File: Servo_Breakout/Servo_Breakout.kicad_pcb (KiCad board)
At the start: 4 copper layers, 96.5 x 31 mm, 52 parts, among them J101 395221002, J102 Conn_01x03, J103 Conn_01x04, Q101 2N7002, U101 TVS0500DRV, U301 STPS15H100CBY-TR, U302 BD9G500EFJ-LAE2, U401 TXS0102DCT, U501 ICM7555xP, U502 TPL0401A-10-Q1

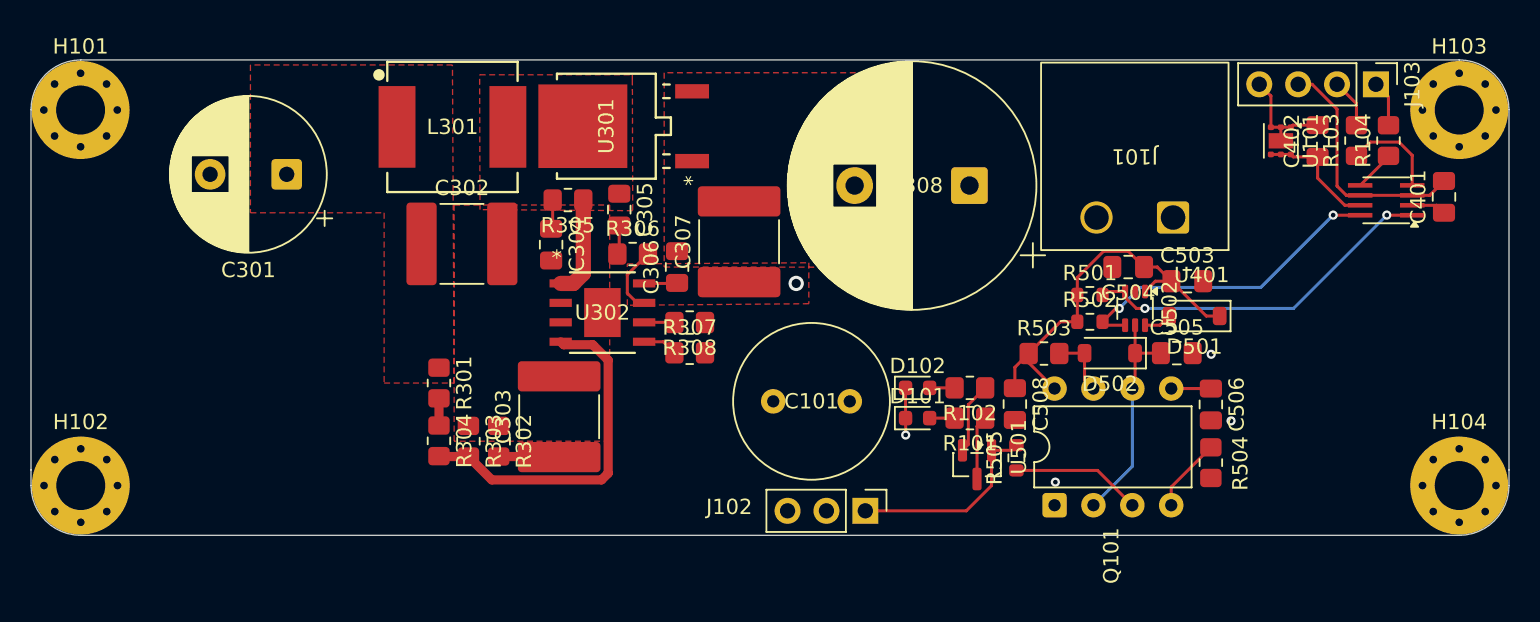
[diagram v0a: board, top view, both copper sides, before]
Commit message: Finalized layout and silkscreen
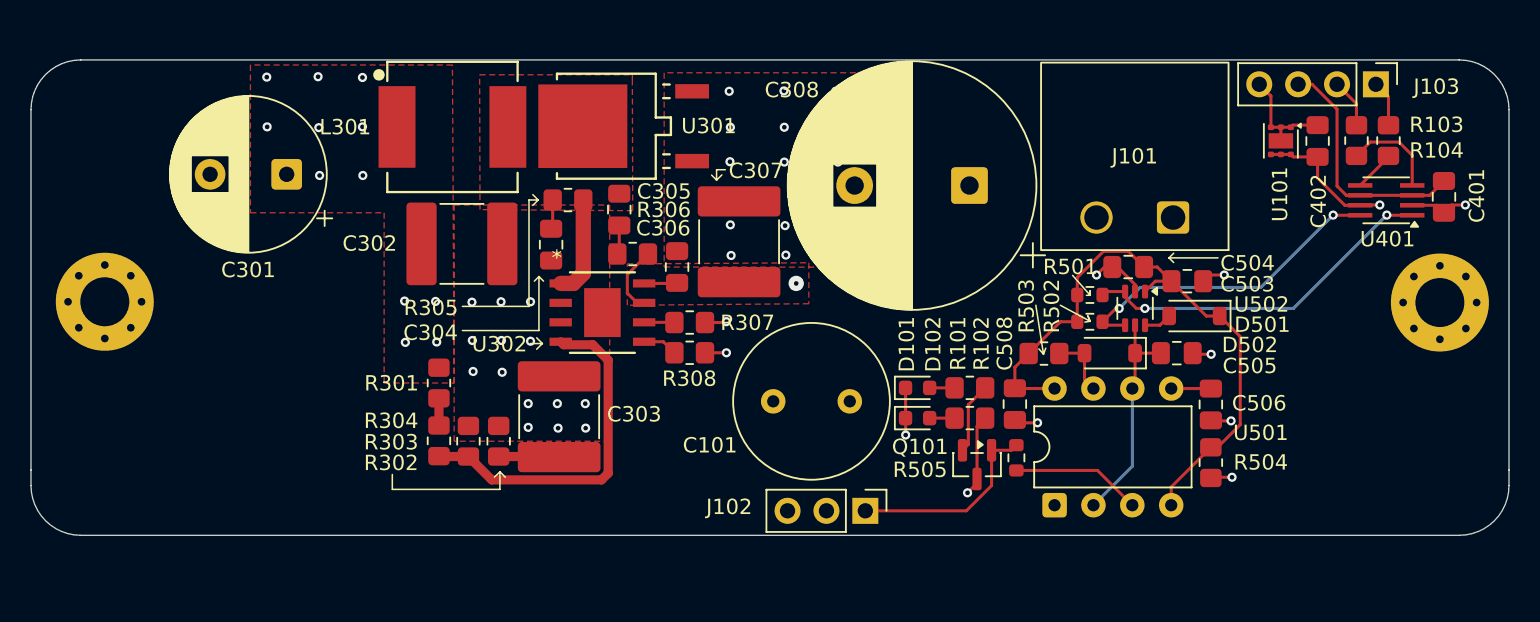
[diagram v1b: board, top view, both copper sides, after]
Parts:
- removed the H101 at (58.9, 54.2)
- removed H103: M3, MountingHole:MountingHole_3.2mm_M3_Pad_Via
- moved H101 12.1 mm to (60.5, 66.8)
- moved H102 12.0 mm to (147.7, 66.8)
- renumbered H102 to H101, H104 to H102
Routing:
- net GND: track 16.4 -> 30.1 mm, vias 4 -> 38
- net /Timer/VCC: track 31.2 -> 41.0 mm
- net /VBUCK: track 12.2 -> 16.1 mm, vias 0 -> 15

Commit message: quick improvement to +36 pour clearance
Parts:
- moved R307 0.70 mm to (98.7, 70.8)
- moved R308 0.70 mm to (98.7, 68.8)
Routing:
- net Net-(U302-FB): track 22.9 -> 28.5 mm
- net Net-(U302-BOOT): track 4.48 -> 8.79 mm, vias 0 -> 2
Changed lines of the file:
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@@
 	(footprint "Resistor_SMD:R_0805_2012Metric_Pad1.20x1.40mm_HandSolder"
 		(layer "F.Cu")
-		(at 98.695 68.129 180)
+		(at 98.675 68.825 180)
 		(descr "Resistor SMD 0805 (2012 Metric), square (rectangular) end terminal, IPC-7351 nominal with elongated pad for handsoldering. (Body size source: IPC-SM-782 page 72, https://www.pcb-3d.com/wordpress/wp-content/uploads/ipc-sm-782a_amendment_1_and_2.pdf), generated with kicad-footprint-generator")
 		(tags "resistor handsolder")
@@
 	(footprint "Resistor_SMD:R_0805_2012Metric_Pad1.20x1.40mm_HandSolder"
 		(layer "F.Cu")
-		(at 98.695 70.104)
+		(at 98.675 70.8)
 		(descr "Resistor SMD 0805 (2012 Metric), square (rectangular) end terminal, IPC-7351 nominal with elongated pad for handsoldering. (Body size source: IPC-SM-782 page 72, https://www.pcb-3d.com/wordpress/wp-content/uploads/ipc-sm-782a_amendment_1_and_2.pdf), generated with kicad-footprint-generator")
 		(tags "resistor handsolder")
@@
 	)
 	(segment
-		(start 147.955 60.96)
-		(end 147.4675 60.4725)
+		(start 99.675 68.825)
+		(end 101.074 68.825)
 		(width 0.2)
 		(layer "F.Cu")
@@
 	)
 	(segment
-		(start 99.695 70.104)
-		(end 101.092 70.104)
+		(start 147.955 60.96)
+		(end 147.4675 60.4725)
 		(width 0.2)
 		(layer "F.Cu")
@@
 	)
 	(segment
-		(start 99.695 68.129)
-		(end 101.035 68.129)
+		(start 101.074 68.825)
+		(end 101.092 68.843)
 		(width 0.2)
 		(layer "F.Cu")
@@
 	)
 	(segment
-		(start 101.035 68.129)
-		(end 101.092 68.072)
-		(width 0.2)
-		(layer "F.Cu")
-		(net 1)
-	)
-	(segment
 		(start 132.7653 74.55)
 		(end 132.7313 74.516)
@@
 	)
 	(segment
+		(start 99.675 70.8)
+		(end 101.017 70.8)
+		(width 0.2)
+		(layer "F.Cu")
+		(net 1)
+	)
+	(segment
 		(start 127.7813 66.1035)
 		(end 127.7813 65.653501)
@@
 		(net 1)
 	)
+	(segment
+		(start 101.017 70.8)
+		(end 101.092 70.875)
+		(width 0.2)
+		(layer "F.Cu")
+		(net 1)
+	)
 	(via
 		(at 101.4 63.75)
@@
 	)
 	(via
-		(at 101.092 70.104)
+		(at 101.092 70.875)
 		(size 0.6)
 		(drill 0.3)
@@
 	)
 	(via
-		(at 101.092 68.072)
+		(at 101.092 68.843)
 		(size 0.6)
 		(drill 0.3)
@@
 	)
 	(segment
-		(start 95.719752 68.114)
-		(end 97.68 68.114)
+		(start 96.964 68.114)
+		(end 97.675 68.825)
 		(width 0.2)
 		(layer "F.Cu")
@@
 	)
 	(segment
-		(start 97.68 68.114)
-		(end 97.695 68.129)
+		(start 95.719752 68.114)
+		(end 96.964 68.114)
 		(width 0.2)
 		(layer "F.Cu")
@@
 	)
 	(segment
-		(start 84.245 76.879)
-		(end 82.345 76.879)
+		(start 90.359 69.384)
+		(end 90.9 69.925)
 		(width 0.6)
 		(layer "F.Cu")
@@
 	)
 	(segment
-		(start 93.371 77.972002)
-		(end 92.938002 78.405)
+		(start 82.32 76.854)
+		(end 84.22 76.854)
 		(width 0.6)
 		(layer "F.Cu")
@@
 	)
 	(segment
-		(start 92.938002 78.405)
-		(end 85.771 78.405)
+		(start 84.245 77.82)
+		(end 84.245 76.879)
 		(width 0.6)
 		(layer "F.Cu")
@@
 	)
 	(segment
-		(start 93.371 70.585998)
-		(end 93.371 77.972002)
+		(start 86.75 80.325)
+		(end 84.245 77.82)
 		(width 0.6)
 		(layer "F.Cu")
@@
 	)
 	(segment
-		(start 92.365202 69.5802)
-		(end 93.371 70.585998)
+		(start 84.22 76.854)
+		(end 84.245 76.879)
 		(width 0.6)
 		(layer "F.Cu")
@@
 	)
 	(segment
-		(start 85.771 78.405)
-		(end 84.245 76.879)
+		(start 93.35 80.325)
+		(end 86.75 80.325)
 		(width 0.6)
 		(layer "F.Cu")
@@
 	(segment
 		(start 90.270248 69.384)
-		(end 90.466448 69.5802)
+		(end 90.359 69.384)
 		(width 0.6)
 		(layer "F.Cu")
@@
 	)
 	(segment
-		(start 90.466448 69.5802)
-		(end 92.365202 69.5802)
+		(start 90.9 69.925)
+		(end 93.575 69.925)
 		(width 0.6)
 		(layer "F.Cu")
@@
 	)
 	(segment
-		(start 82.345 76.879)
-		(end 82.32 76.854)
+		(start 95.35 71.7)
+		(end 95.35 78.325)
 		(width 0.6)
 		(layer "F.Cu")
@@
 	)
 	(segment
-		(start 95.97 63.654)
-		(end 94.62 65.004)
+		(start 95.35 78.325)
+		(end 93.35 80.325)
+		(width 0.6)
+		(layer "F.Cu")
+		(net 44)
+	)
+	(segment
+		(start 93.575 69.925)
+		(end 95.35 71.7)
+		(width 0.6)
+		(layer "F.Cu")
+		(net 44)
+	)
+	(segment
+		(start 95.719752 66.969752)
+		(end 95.9 67.15)
 		(width 0.2)
 		(layer "F.Cu")
@@
 	)
 	(segment
-		(start 94.62 65.004)
-		(end 94.62 66.208398)
+		(start 95.9 67.15)
+		(end 96.1 67.35)
 		(width 0.2)
 		(layer "F.Cu")
@@
 	)
 	(segment
-		(start 94.62 66.208398)
-		(end 95.255602 66.844)
+		(start 96.1 67.35)
+		(end 97.1 67.35)
+		(width 0.2)
+		(layer "F.Cu")
+		(net 45)
+	)
+	(segment
+		(start 95.719752 66.844)
+		(end 95.719752 66.969752)
+		(width 0.2)
+		(layer "F.Cu")
+		(net 45)
+	)
+	(segment
+		(start 95.97 63.654)
+		(end 95.97 62.405)
 		(width 0.2)
 		(layer "F.Cu")
@@
 		(net 45)
 	)
+	(via
+		(at 97.1 67.35)
+		(size 0.6)
+		(drill 0.3)
+		(layers "F.Cu" "B.Cu")
+		(net 45)
+	)
+	(via
+		(at 95.97 62.405)
+		(size 0.6)
+		(drill 0.3)
+		(layers "F.Cu" "B.Cu")
+		(net 45)
+	)
 	(segment
-		(start 95.719752 69.384)
-		(end 96.975 69.384)
+		(start 97.1 67.35)
+		(end 97.1 63.535)
+		(width 0.2)
+		(layer "B.Cu")
+		(net 45)
+	)
+	(segment
+		(start 97.1 63.535)
+		(end 95.97 62.405)
+		(width 0.2)
+		(layer "B.Cu")
+		(net 45)
+	)
+	(segment
+		(start 96.259 69.384)
+		(end 97.675 70.8)
 		(width 0.2)
 		(layer "F.Cu")
@@
 	)
 	(segment
-		(start 96.975 69.384)
-		(end 97.695 70.104)
+		(start 95.719752 69.384)
+		(end 96.259 69.384)
 		(width 0.2)
 		(layer "F.Cu")
@@
 		(priority 6)
 		(connect_pads yes
-			(clearance 0)
+			(clearance 0.5)
 		)
 		(min_thickness 0.25)
@@
 		(hatch edge 0.5)
 		(connect_pads yes
-			(clearance 0)
+			(clearance 0.5)
 		)
 		(min_thickness 0.25)
@@
 		(polygon
 			(pts
-				(xy 94.62 64.3) (xy 106.475 64.225) (xy 106.475 66.9) (xy 94.62 67)
+				(xy 94.62 64.3) (xy 106.475 64.225) (xy 106.475 66.45) (xy 94.62 66.55)
 			)
 		)
@@
 		(priority 3)
 		(connect_pads yes
-			(clearance 0)
+			(clearance 0.4)
 		)
-		(min_thickness 0.25)
+		(min_thickness 0.4)
 		(filled_areas_thickness no)
 		(fill yes
@@
 		(priority 2)
 		(connect_pads yes
-			(clearance 0)
+			(clearance 0.4)
 		)
-		(min_thickness 0.25)
+		(min_thickness 0.4)
 		(filled_areas_thickness no)
 		(fill yes
@@
 		(priority 4)
 		(connect_pads yes
-			(clearance 0)
+			(clearance 0.4)
 		)
-		(min_thickness 0.25)
+		(min_thickness 0.4)
 		(filled_areas_thickness no)
 		(fill yes
@@
 		(priority 5)
 		(connect_pads yes
-			(clearance 0)
+			(clearance 0.25)
 		)
 		(min_thickness 0.25)
@@
 		(priority 5)
 		(connect_pads yes
-			(clearance 0)
+			(clearance 0.25)
 		)
 		(min_thickness 0.25)
@@
 		(priority 1)
 		(connect_pads yes
-			(clearance 0)
+			(clearance 0.25)
 		)
 		(min_thickness 0.25)
@@
 		(polygon
 			(pts
-				(xy 113.275 50.975) (xy 113.3 63.375) (xy 133.875 63.375) (xy 133.875 50.975)
+				(xy 113.25 63.4) (xy 113.25 55) (xy 133.875 55) (xy 133.825 63.4)
 			)
 		)

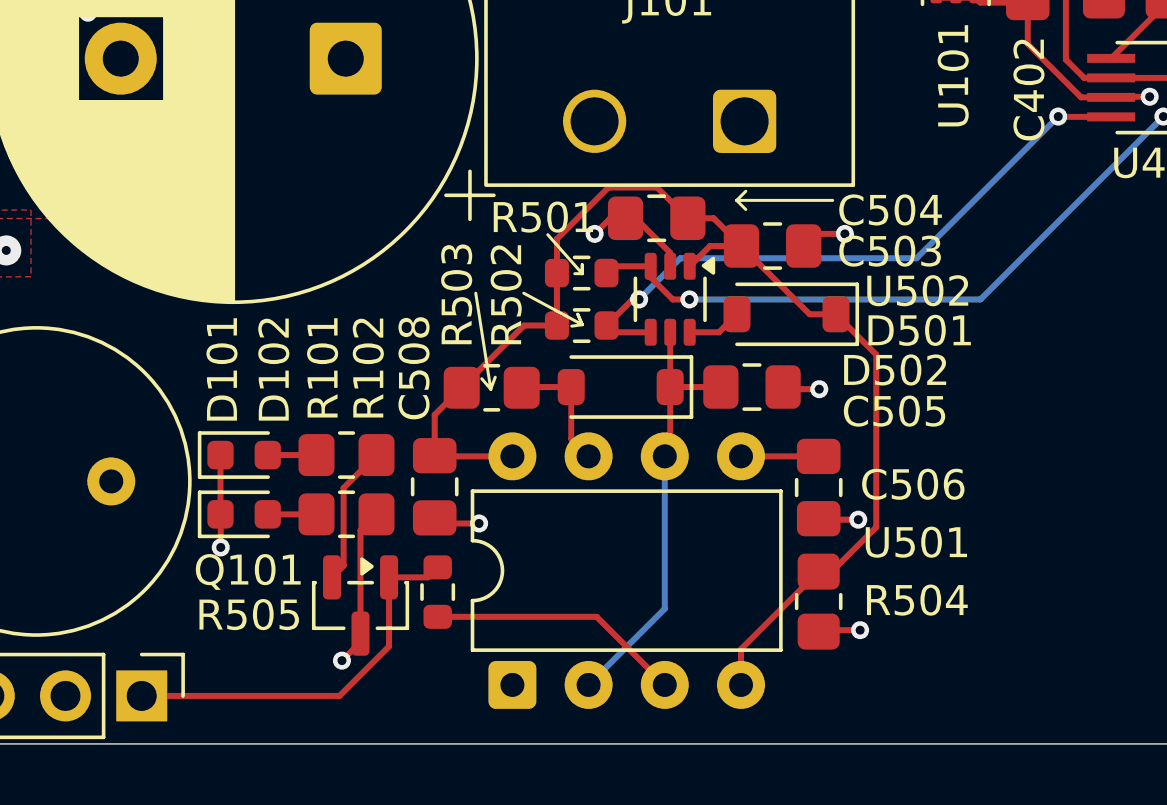
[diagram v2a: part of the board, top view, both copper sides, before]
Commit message: simplify 555 timer circuit. update green_led switch to low-side switching
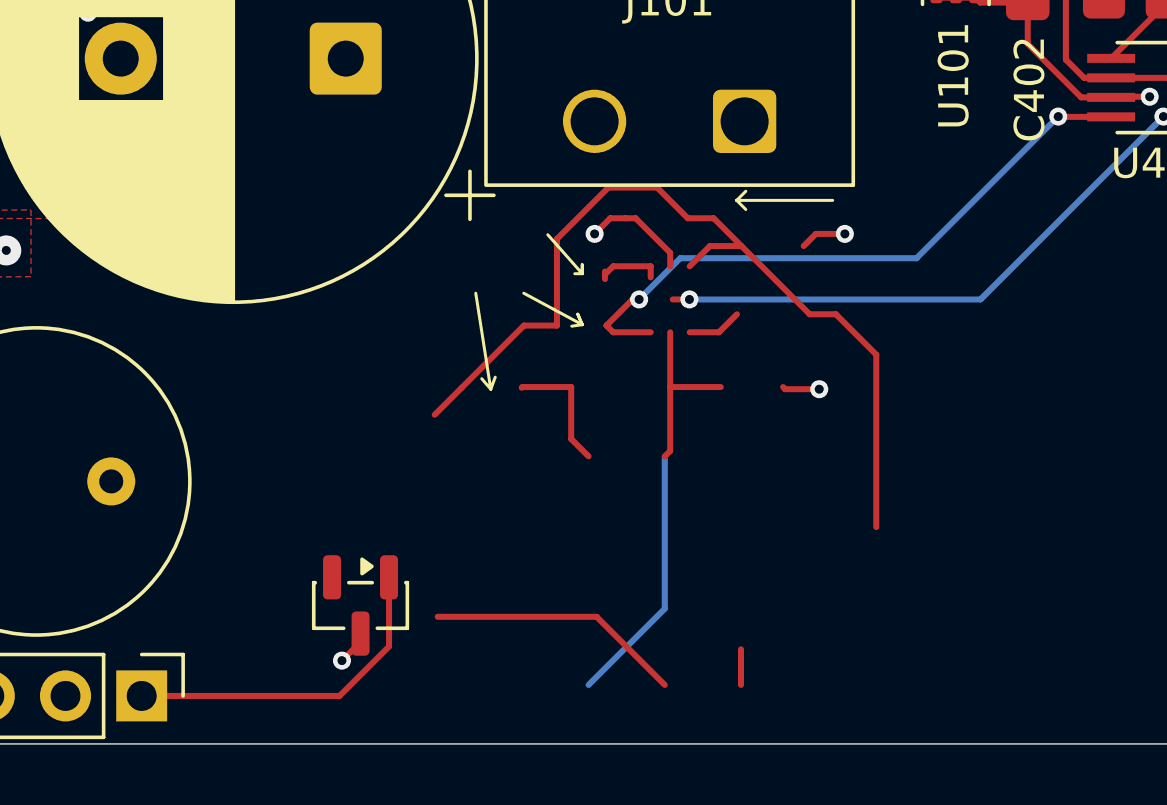
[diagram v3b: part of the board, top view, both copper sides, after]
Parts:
- removed C503, C508: 10uF, Capacitor_SMD:C_0805_2012Metric_Pad1.18x1.45mm_HandSolder
- removed C504, C505: 0.1uF, Capacitor_SMD:C_0805_2012Metric_Pad1.18x1.45mm_HandSolder
- removed C506: 0.1uF/X7R, Capacitor_SMD:C_0805_2012Metric_Pad1.18x1.45mm_HandSolder
- removed D101: RED_LED, LED_SMD:LED_0603_1608Metric
- removed D102: GREEN_LED, LED_SMD:LED_0603_1608Metric
- removed D501, D502: 1N4148W, Diode_SMD:D_SOD-123
- removed R101, R102: 470, Resistor_SMD:R_0805_2012Metric_Pad1.20x1.40mm_HandSolder
- removed R501, R502: 4.7k, Resistor_SMD:R_0603_1608Metric
- removed R503: 150k, Resistor_SMD:R_0805_2012Metric_Pad1.20x1.40mm_HandSolder
- removed R504: 47, Resistor_SMD:R_0805_2012Metric_Pad1.20x1.40mm_HandSolder
- removed R505: 0, Resistor_SMD:R_0603_1608Metric
- removed U501: ICM7555xP, Package_DIP:DIP-8_W7.62mm
- removed U502: TPL0401A-10-Q1, Package_TO_SOT_SMD:Texas_R-PDSO-G6
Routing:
- net /Timer/VCC: track 41.0 -> 30.8 mm
- net GND: track 30.2 -> 24.2 mm, vias 38 -> 35
- net /VBUCK: track 16.1 -> 10.5 mm, vias 15 -> 14
- net /LED_GREEN: track 4.69 -> 0.00 mm
- net Net-(U501-CONT): track 2.59 -> 0.00 mm
- net /PWM_A1: track 13.0 -> 11.2 mm
- net Net-(D102-A): track 1.62 -> 0.00 mm
- net Net-(D101-A): track 1.62 -> 0.00 mm
- net /I2C1_SCL: track 23.8 -> 22.7 mm
